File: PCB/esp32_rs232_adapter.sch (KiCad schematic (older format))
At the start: 8 parts

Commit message: work on schematics
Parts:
- removed C? (x4): CP1_Small, symbol Device:CP1_Small
- added C? (x4): 0.1uF, symbol Device:CP1_Small
- added C?: 1uF, symbol Device:CP1_Small
- added J?: DB9_Male, symbol Connector:DB9_Male
- added R? (x3): 1k, symbol Device:R_Small
- C?: value CP1_Small -> 0.1uF
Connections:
- net GND: now also U?.1 (GND), U?.15 (GND), U?.24 (IO2), U?.38 (GND), C?.1, C?.2, C?.2, C?.2, J?.5
- net RTS: now reaches U?.10 (T2IN)
- net RTS: now also U?.36 (IO22), R?.2
- net TXD: now reaches U?.11 (T1IN)
- net TXD: now also U?.35 (TXD0/IO1), R?.2
- net RXD: now reaches U?.12 (R1OUT)
- net RXD: now also U?.34 (RXD0/IO3)
- net RXD_RS232: now reaches J?.3, U?.13 (R1IN)
- net RXD_RS232: now also J?.2
- net TXD_RS232: now reaches J?.2, U?.14 (T1OUT)
- net TXD_RS232: now also J?.3
- net +3V3: now reaches U?.16 (VCC)
- net +3V3: now also U?.2 (VDD), C?.1, C?.1, R?.1, R?.1, R?.1
- net at U?.2 (VS+): now also C?.1
- net at U?.4 (C2+): now also C?.1
- net at U?.5 (C2-): now also C?.2
- net at U?.6 (VS-): now also C?.2
- net RTS_RS232: now reaches J?.8, U?.7 (T2OUT)
- net RTS_RS232: now also J?.7
- net CTS_RS232: now reaches J?.7, U?.8 (R2IN)
- net CTS_RS232: now also J?.8
- net CTS: now reaches U?.9 (R2OUT)
- net CTS: now also U?.31 (IO19)
- net at U?.25 (IO0): now also R?.2
- new net: J?.1, J?.4, J?.6
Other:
- moved on the sheet: C?, J?, U?

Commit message: Nearly finished schematic
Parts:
- removed R?: 1k, symbol Device:R_Small
- added D3, D4: LED_Small, LED_SMD:LED_0805_2012Metric, symbol Device:LED_Small
- added J1: Conn_01x04_Male, Connector_PinHeader_2.54mm:PinHeader_1x04_P2.54mm_Vertical, symbol Connector:Conn_01x04_Male
- added R1, R12, R13, R2, R5: 10k, Resistor_SMD:R_0805_2012Metric, symbol Device:R_Small
- added SW1: Flash, Button_Switch_SMD:SW_SPST_B3S-1000, symbol Switch:SW_Push
- C1: renamed from C?; value 1uF -> 10uF; footprint (none) -> Capacitor_SMD:C_0805_2012Metric
- C2, C3, C4, C5, C6: renamed from C?; footprint (none) -> Capacitor_SMD:C_0805_2012Metric
- J2: renamed from J?; value DB9_Male -> DB9; footprint (none) -> Connector_Dsub:DSUB-9_Male_Horizontal_P2.77x2.54mm_EdgePinOffset9.40mm; Supplier (none) -> https://www.aliexpress.com/item/DB9-Female-PCB-Mount-D-Sub-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
- J3: renamed from J?; value DB9_Male -> DB9X; footprint (none) -> Connector_Dsub:DSUB-9_Male_Horizontal_P2.77x2.54mm_EdgePinOffset9.40mm; Supplier (none) -> https://www.aliexpress.com/item/DB9-Female-PCB-Mount-D-Sub-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
- R3, R4: renamed from R?; value 1k -> 10k; footprint (none) -> Resistor_SMD:R_0805_2012Metric
- U1: renamed from U?; Supplier (none) -> https://www.aliexpress.com/item/ESP32-WROOM-32D-ESP32-D0WD-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
- U2: renamed from U?; footprint (none) -> Package_SO:SSOP-16_5.3x6.2mm_P0.65mm; Supplier (none) -> https://www.aliexpress.com/item/in-stock-can-pay-MAX3232CSE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
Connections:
- wire segments 93 -> 113
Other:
- moved on the sheet: C1, R3

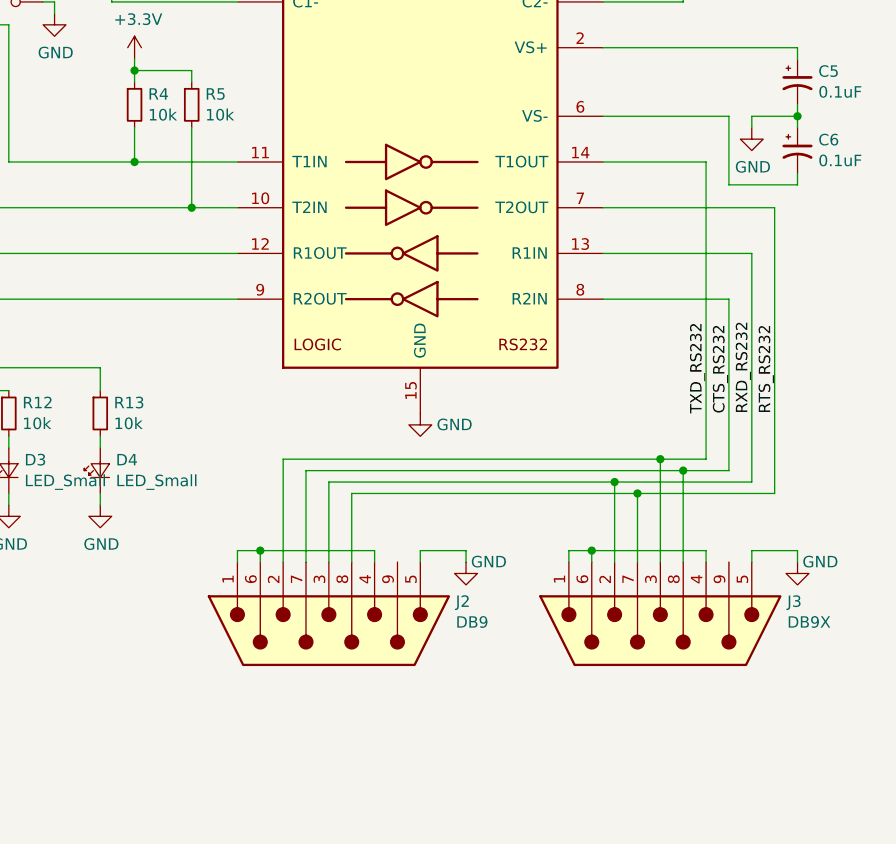
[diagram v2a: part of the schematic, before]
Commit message: change footprints. Add dip switch for null modem
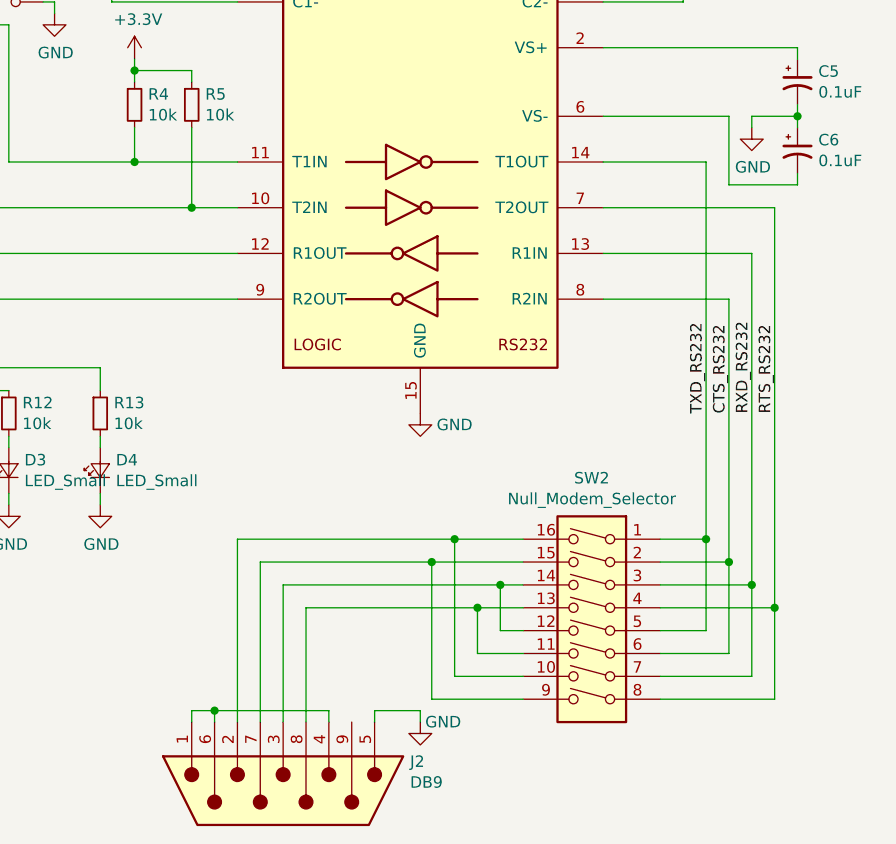
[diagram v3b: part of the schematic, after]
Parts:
- removed J3: DB9X, Connector_Dsub:DSUB-9_Male_Horizontal_P2.77x2.54mm_EdgePinOffset9.40mm, symbol Connector:DB9_Male
- added SW2: Null_Modem_Selector, Button_Switch_SMD:SW_DIP_SPSTx08_Slide_6.7x21.88mm_W8.61mm_P2.54mm_LowProfile, symbol Switch:SW_DIP_x08
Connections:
- wire segments 113 -> 121
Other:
- moved on the sheet: J2
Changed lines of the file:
@@
 L Connector:DB9_Male J2
 U 1 1 5C74F18C
-P 8600 5350
-F 0 "J2" V 8473 5905 50  0000 L CNN
-F 1 "DB9" V 8564 5905 50  0000 L CNN
-F 2 "Connector_Dsub:DSUB-9_Male_Horizontal_P2.77x2.54mm_EdgePinOffset9.40mm" H 8600 5350 50  0001 C CNN
-F 3 " ~" H 8600 5350 50  0001 C CNN
-F 4 "https://www.aliexpress.com/item/DB9-Female-PCB-Mount-D-Sub-9-pin-PCB-Connector-RS232-Connector-90-degree-bent-needle/32829295480.html" V 8600 5350 50  0001 C CNN "Supplier"
-	1    8600 5350
+P 8400 6050
+F 0 "J2" V 8273 6605 50  0000 L CNN
+F 1 "DB9" V 8364 6605 50  0000 L CNN
+F 2 "Connector_Dsub:DSUB-9_Male_Horizontal_P2.77x2.54mm_EdgePinOffset9.40mm" H 8400 6050 50  0001 C CNN
+F 3 " ~" H 8400 6050 50  0001 C CNN
+F 4 "https://www.aliexpress.com/item/DB9-Female-PCB-Mount-D-Sub-9-pin-PCB-Connector-RS232-Connector-90-degree-bent-needle/32829295480.html" V 8400 6050 50  0001 C CNN "Supplier"
+	1    8400 6050
 	0    1    1    0
 $EndComp
@@
 	10450 3100 10650 3100
 Wire Wire Line
-	8200 5050 8200 5000
-Wire Wire Line
-	8200 5000 8300 5000
-Wire Wire Line
-	8300 5000 8300 5050
-Wire Wire Line
-	8300 5000 8800 5000
-Wire Wire Line
-	8800 5000 8800 5050
-Connection ~ 8300 5000
-Wire Wire Line
-	9000 5050 9000 5000
-Wire Wire Line
-	9000 5000 9200 5000
+	8000 5750 8000 5700
+Wire Wire Line
+	8000 5700 8100 5700
+Wire Wire Line
+	8100 5700 8100 5750
+Wire Wire Line
+	8100 5700 8600 5700
+Wire Wire Line
+	8600 5700 8600 5750
+Connection ~ 8100 5700
+Wire Wire Line
+	8800 5750 8800 5700
+Wire Wire Line
+	8800 5700 9000 5700
 $Comp
 L power:GND #PWR014
 U 1 1 5C752181
-P 9200 5050
-F 0 "#PWR014" H 9200 4800 50  0001 C CNN
-F 1 "GND" H 9300 5050 50  0000 C CNN
-F 2 "" H 9200 5050 50  0001 C CNN
-F 3 "" H 9200 5050 50  0001 C CNN
-	1    9200 5050
-	1    0    0    -1
-$EndComp
-Wire Wire Line
-	8700 5050 8700 4750
-Wire Wire Line
-	10550 4750 10550 3500
+P 9000 5750
+F 0 "#PWR014" H 9000 5500 50  0001 C CNN
+F 1 "GND" H 9100 5750 50  0000 C CNN
+F 2 "" H 9000 5750 50  0001 C CNN
+F 3 "" H 9000 5750 50  0001 C CNN
+	1    9000 5750
+	1    0    0    -1
+$EndComp
+Wire Wire Line
+	8500 5750 8500 5250
 Wire Wire Line
 	10550 3500 9800 3500
@@
 	9800 3900 10350 3900
 Wire Wire Line
-	10350 3900 10350 4650
-Wire Wire Line
-	8500 4650 8500 5050
-Wire Wire Line
-	8400 5050 8400 4600
-Wire Wire Line
-	8400 4600 10050 4600
-Wire Wire Line
-	10250 4600 10250 3300
+	8200 5750 8200 4950
 Wire Wire Line
 	10250 3300 9800 3300
 Wire Wire Line
-	8600 5050 8600 4700
-Wire Wire Line
-	10450 4700 10450 3700
+	8400 5750 8400 5150
 Wire Wire Line
 	10450 3700 9800 3700
@@
 RTS_RS232
 Wire Wire Line
-	9200 5000 9200 5050
-$Comp
-L Connector:DB9_Male J3
-U 1 1 5C7F8A3E
-P 10050 5350
-F 0 "J3" V 9923 5905 50  0000 L CNN
-F 1 "DB9X" V 10014 5905 50  0000 L CNN
-F 2 "Connector_Dsub:DSUB-9_Male_Horizontal_P2.77x2.54mm_EdgePinOffset9.40mm" H 10050 5350 50  0001 C CNN
-F 3 " ~" H 10050 5350 50  0001 C CNN
-F 4 "https://www.aliexpress.com/item/DB9-Female-PCB-Mount-D-Sub-9-pin-PCB-Connector-RS232-Connector-90-degree-bent-needle/32829295480.html" V 10050 5350 50  0001 C CNN "Supplier"
-	1    10050 5350
-	0    1    1    0
-$EndComp
-Wire Wire Line
-	9650 5050 9650 5000
-Wire Wire Line
-	9650 5000 9750 5000
-Wire Wire Line
-	9750 5000 9750 5050
-Wire Wire Line
-	9750 5000 10250 5000
-Wire Wire Line
-	10250 5000 10250 5050
-Connection ~ 9750 5000
-Wire Wire Line
-	10450 5050 10450 5000
-Wire Wire Line
-	10450 5000 10650 5000
-$Comp
-L power:GND #PWR017
-U 1 1 5C7F8A4D
-P 10650 5050
-F 0 "#PWR017" H 10650 4800 50  0001 C CNN
-F 1 "GND" H 10750 5050 50  0000 C CNN
-F 2 "" H 10650 5050 50  0001 C CNN
-F 3 "" H 10650 5050 50  0001 C CNN
-	1    10650 5050
-	1    0    0    -1
-$EndComp
-Wire Wire Line
-	10650 5000 10650 5050
-Wire Wire Line
-	8500 4650 10150 4650
-Wire Wire Line
-	8700 4750 9950 4750
-Wire Wire Line
-	8600 4700 9850 4700
-Wire Wire Line
-	10250 4600 10050 4600
-Wire Wire Line
-	10050 4600 10050 5050
-Connection ~ 10050 4600
-Wire Wire Line
-	9850 4700 9850 5050
-Connection ~ 9850 4700
-Wire Wire Line
-	9850 4700 10450 4700
-Wire Wire Line
-	10150 4650 10150 5050
-Connection ~ 10150 4650
-Wire Wire Line
-	10150 4650 10350 4650
-Wire Wire Line
-	9950 4750 9950 5050
-Connection ~ 9950 4750
-Wire Wire Line
-	9950 4750 10550 4750
+	9000 5700 9000 5750
 $Comp
 L power:+3.3V #PWR04
@@
 	0    -1   -1   0
 $EndComp
+$Comp
+L Switch:SW_DIP_x08 SW2
+U 1 1 5C88E389
+P 9750 5350
+F 0 "SW2" H 9750 6017 50  0000 C CNN
+F 1 "Null_Modem_Selector" H 9750 5926 50  0000 C CNN
+F 2 "Button_Switch_SMD:SW_DIP_SPSTx08_Slide_6.7x21.88mm_W8.61mm_P2.54mm_LowProfile" H 9750 5350 50  0001 C CNN
+F 3 "https://www.aliexpress.com/item/10pcs-lot-Slide-Type-SMT-SMD-Dip-Switch-2-54mm-Pitch-2-Row-4-Pin-2/32956815576.html" H 9750 5350 50  0001 C CNN
+	1    9750 5350
+	-1   0    0    -1
+$EndComp
+Wire Wire Line
+	10250 4950 10050 4950
+Wire Wire Line
+	9450 4950 9150 4950
+Wire Wire Line
+	10250 3300 10250 4950
+Wire Wire Line
+	10250 4950 10250 5350
+Wire Wire Line
+	10250 5350 10050 5350
+Connection ~ 10250 4950
+Wire Wire Line
+	10350 5050 10050 5050
+Wire Wire Line
+	10350 5050 10350 5450
+Wire Wire Line
+	10350 5450 10050 5450
+Connection ~ 10350 5050
+Wire Wire Line
+	10450 5150 10050 5150
+Wire Wire Line
+	10450 5150 10450 5550
+Wire Wire Line
+	10450 5550 10050 5550
+Connection ~ 10450 5150
+Wire Wire Line
+	10550 5250 10050 5250
+Wire Wire Line
+	10550 5250 10550 5650
+Wire Wire Line
+	10550 5650 10050 5650
+Connection ~ 10550 5250
+Wire Wire Line
+	9450 5050 9050 5050
+Wire Wire Line
+	8300 5050 8300 5750
+Wire Wire Line
+	10350 3900 10350 5050
+Wire Wire Line
+	9450 5150 9350 5150
+Wire Wire Line
+	10450 3700 10450 5150
+Wire Wire Line
+	9450 5250 9250 5250
+Wire Wire Line
+	10550 3500 10550 5250
+Wire Wire Line
+	9450 5350 9350 5350
+Wire Wire Line
+	9350 5350 9350 5150
+Connection ~ 9350 5150
+Wire Wire Line
+	9350 5150 8400 5150
+Wire Wire Line
+	9450 5550 9150 5550
+Wire Wire Line
+	9150 5550 9150 4950
+Connection ~ 9150 4950
+Wire Wire Line
+	9150 4950 8200 4950
+Wire Wire Line
+	9450 5450 9250 5450
+Wire Wire Line
+	9250 5450 9250 5250
+Connection ~ 9250 5250
+Wire Wire Line
+	9250 5250 8500 5250
+Wire Wire Line
+	9450 5650 9050 5650
+Wire Wire Line
+	9050 5650 9050 5050
+Connection ~ 9050 5050
+Wire Wire Line
+	9050 5050 8300 5050
 $EndSCHEMATC

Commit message: PCB finished
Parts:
- added H1, H2, H3, H4: MountingHole, MountingHole:MountingHole_3.2mm_M3_ISO7380, symbol Mechanical:MountingHole
- J2: footprint Connector_Dsub:DSUB-9_Male_Horizontal_P2.77x2.54mm_EdgePinOffset9.40mm -> Connector_Dsub:DSUB-9_Male_Horizontal_P2.77x2.84mm_EdgePinOffset4.94mm_Housed_MountingHolesOffset7.48mm
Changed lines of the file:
@@
 F 0 "J2" V 8273 6605 50  0000 L CNN
 F 1 "DB9" V 8364 6605 50  0000 L CNN
-F 2 "Connector_Dsub:DSUB-9_Male_Horizontal_P2.77x2.54mm_EdgePinOffset9.40mm" H 8400 6050 50  0001 C CNN
+F 2 "Connector_Dsub:DSUB-9_Male_Horizontal_P2.77x2.84mm_EdgePinOffset4.94mm_Housed_MountingHolesOffset7.48mm" H 8400 6050 50  0001 C CNN
 F 3 " ~" H 8400 6050 50  0001 C CNN
 F 4 "https://www.aliexpress.com/item/DB9-Female-PCB-Mount-D-Sub-9-pin-PCB-Connector-RS232-Connector-90-degree-bent-needle/32829295480.html" V 8400 6050 50  0001 C CNN "Supplier"
@@
 Wire Wire Line
 	9050 5050 8300 5050
+$Comp
+L Mechanical:MountingHole H?
+U 1 1 5C979F20
+P 950 850
+AR Path="/5C7BB31A/5C979F20" Ref="H?"  Part="1"
+AR Path="/5C979F20" Ref="H1"  Part="1"
+F 0 "H1" H 1050 896 50  0000 L CNN
+F 1 "MountingHole" H 1050 805 50  0000 L CNN
+F 2 "MountingHole:MountingHole_3.2mm_M3_ISO7380" H 950 850 50  0001 C CNN
+F 3 "~" H 950 850 50  0001 C CNN
+	1    950  850
+	1    0    0    -1
+$EndComp
+$Comp
+L Mechanical:MountingHole H?
+U 1 1 5C979F27
+P 950 1050
+AR Path="/5C7BB31A/5C979F27" Ref="H?"  Part="1"
+AR Path="/5C979F27" Ref="H2"  Part="1"
+F 0 "H2" H 1050 1096 50  0000 L CNN
+F 1 "MountingHole" H 1050 1005 50  0000 L CNN
+F 2 "MountingHole:MountingHole_3.2mm_M3_ISO7380" H 950 1050 50  0001 C CNN
+F 3 "~" H 950 1050 50  0001 C CNN
+	1    950  1050
+	1    0    0    -1
+$EndComp
+$Comp
+L Mechanical:MountingHole H?
+U 1 1 5C979F2E
+P 950 1250
+AR Path="/5C7BB31A/5C979F2E" Ref="H?"  Part="1"
+AR Path="/5C979F2E" Ref="H3"  Part="1"
+F 0 "H3" H 1050 1296 50  0000 L CNN
+F 1 "MountingHole" H 1050 1205 50  0000 L CNN
+F 2 "MountingHole:MountingHole_3.2mm_M3_ISO7380" H 950 1250 50  0001 C CNN
+F 3 "~" H 950 1250 50  0001 C CNN
+	1    950  1250
+	1    0    0    -1
+$EndComp
+$Comp
+L Mechanical:MountingHole H?
+U 1 1 5C979F35
+P 950 1450
+AR Path="/5C7BB31A/5C979F35" Ref="H?"  Part="1"
+AR Path="/5C979F35" Ref="H4"  Part="1"
+F 0 "H4" H 1050 1496 50  0000 L CNN
+F 1 "MountingHole" H 1050 1405 50  0000 L CNN
+F 2 "MountingHole:MountingHole_3.2mm_M3_ISO7380" H 950 1450 50  0001 C CNN
+F 3 "~" H 950 1450 50  0001 C CNN
+	1    950  1450
+	1    0    0    -1
+$EndComp
 $EndSCHEMATC

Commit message: update
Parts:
- removed J1: Conn_01x04_Male, Connector_PinHeader_2.54mm:PinHeader_1x04_P2.54mm_Vertical, symbol Connector:Conn_01x04_Male
- U2: footprint Package_SO:SSOP-16_5.3x6.2mm_P0.65mm -> Package_SO:SOP-16_4.55x10.3mm_P1.27mm
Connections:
- wire segments 121 -> 126
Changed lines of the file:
@@
 EESchema Schematic File Version 4
 LIBS:esp32_rs232_adapter-cache
-EELAYER 26 0
+EELAYER 29 0
 EELAYER END
 $Descr A4 11693 8268
@@
 F 0 "U2" H 9000 4578 50  0000 C CNN
 F 1 "MAX3232" H 9000 4487 50  0000 C CNN
-F 2 "Package_SO:SSOP-16_5.3x6.2mm_P0.65mm" H 9050 2150 50  0001 L CNN
+F 2 "Package_SO:SOP-16_4.55x10.3mm_P1.27mm" H 9050 2150 50  0001 L CNN
 F 3 "https://datasheets.maximintegrated.com/en/ds/MAX3222-MAX3241.pdf" H 9000 3300 50  0001 C CNN
 F 4 "https://www.aliexpress.com/item/in-stock-can-pay-MAX3232CSE-MAX3232-MAX3232ESE-SOP-16/32821460559.html" H 9000 3200 50  0001 C CNN "Supplier"
@@
 F2 "3.3V" I R 3950 2500 50
 F3 "Vbatt_sig" I R 3950 2800 50
+F4 "power_status" I R 3950 3050 50
+F5 "charge_status" I R 3950 3150 50
 $EndSheet
 Wire Wire Line
@@
 Wire Wire Line
 	3950 2800 5400 2800
-$Comp
-L Connector:Conn_01x04_Male J1
-U 1 1 5C7F4A31
-P 2700 4350
-F 0 "J1" H 2806 4628 50  0000 C CNN
-F 1 "Conn_01x04_Male" H 2806 4537 50  0000 C CNN
-F 2 "Connector_PinHeader_2.54mm:PinHeader_1x04_P2.54mm_Vertical" H 2700 4350 50  0001 C CNN
-F 3 "~" H 2700 4350 50  0001 C CNN
-	1    2700 4350
-	1    0    0    -1
-$EndComp
-Wire Wire Line
-	2900 4250 3350 4250
-Wire Wire Line
-	2900 4350 3350 4350
-Wire Wire Line
-	2900 4550 3350 4550
-$Comp
-L power:GND #PWR01
-U 1 1 5C8018A8
-P 3350 4600
-F 0 "#PWR01" H 3350 4350 50  0001 C CNN
-F 1 "GND" H 3355 4427 50  0000 C CNN
-F 2 "" H 3350 4600 50  0001 C CNN
-F 3 "" H 3350 4600 50  0001 C CNN
-	1    3350 4600
-	1    0    0    -1
-$EndComp
-Wire Wire Line
-	3350 4600 3350 4550
-$Comp
-L power:+3.3V #PWR02
-U 1 1 5C804F12
-P 3550 4450
-F 0 "#PWR02" H 3550 4300 50  0001 C CNN
-F 1 "+3.3V" H 3565 4623 50  0000 C CNN
-F 2 "" H 3550 4450 50  0001 C CNN
-F 3 "" H 3550 4450 50  0001 C CNN
-	1    3550 4450
-	1    0    0    -1
-$EndComp
-Wire Wire Line
-	2900 4450 3550 4450
-Text Label 3350 4350 2    50   ~ 0
-TXD
-Text Label 3350 4250 2    50   ~ 0
-RXD
 $Comp
 L Device:LED_Small D3
@@
 	1    0    0    -1
 $EndComp
+Wire Wire Line
+	3950 3050 4800 3050
+Wire Wire Line
+	4800 3050 4800 5400
+Wire Wire Line
+	4800 5400 6700 5400
+Wire Wire Line
+	6700 5400 6700 4900
+Wire Wire Line
+	6700 4900 6600 4900
+Wire Wire Line
+	3950 3150 4700 3150
+Wire Wire Line
+	4700 3150 4700 5500
+Wire Wire Line
+	4700 5500 6750 5500
+Wire Wire Line
+	6750 5500 6750 4800
+Wire Wire Line
+	6750 4800 6600 4800
 $EndSCHEMATC

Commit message: work in progress with stuff for cb testing
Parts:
- added C12, C14, C17: 0.1uF, Capacitor_SMD:C_0805_2012Metric, symbol Device:CP1_Small
- added C13: 1nF, Capacitor_SMD:C_0805_2012Metric, symbol Device:CP1_Small
- added C15: 10nF, Capacitor_SMD:C_0805_2012Metric, symbol Device:CP1_Small
- added C16: 0.1nF, Capacitor_SMD:C_0805_2012Metric, symbol Device:CP1_Small
- added C18: 2.2nF, Capacitor_SMD:C_0805_2012Metric, symbol Device:CP1_Small
- added J3: Shunt-, Connector:Banana_Jack_1Pin, symbol Connector:Conn_01x01_Female
- added J4: Poles, Connector:Banana_Jack_3Pin, symbol Connector:Conn_01x03_Female
- added J5: Common, Connector:Banana_Jack_1Pin, symbol Connector:Conn_01x01_Female
- added J6: Shunt+, Connector:Banana_Jack_1Pin, symbol Connector:Conn_01x01_Female
- added R15: 3k3, Resistor_SMD:R_0805_2012Metric, symbol Device:R_Small
- added R16, R17, R18: 10k, Resistor_SMD:R_0805_2012Metric, symbol Device:R_Small
- added U5: ACS712xLCTR-30A, Package_SO:SOIC-8_3.9x4.9mm_P1.27mm, symbol Sensor_Current:ACS712xLCTR-30A
- added U6: MPU-6050, Sensor_Motion:InvenSense_QFN-24_4x4mm_P0.5mm, symbol Sensor_Motion:MPU-6050
- U1: footprint RF_Module:ESP32-WROOM-32 -> power_supplies:ESP32-WROOM-32-Heat
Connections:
- net labels added: Aph, Bph, ChargePwrStatus, ChargeStatus, Cph, External+, External-, I_sense, Vbatt_sig, mpu_INT, mpu_SCL, mpu_SDA
- wire segments 126 -> 194
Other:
- moved on the sheet: C1, C2, C3, C4, C5, C6, D3, D4, J2, R1, R12, R13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

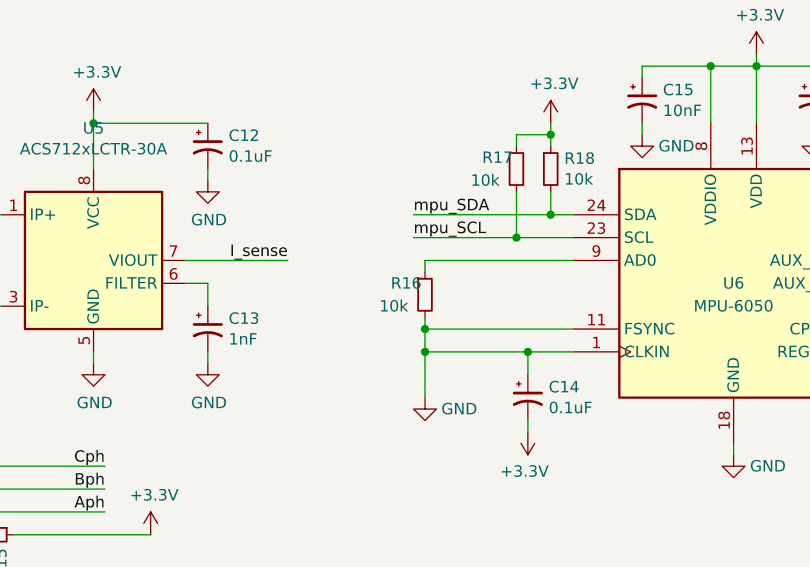
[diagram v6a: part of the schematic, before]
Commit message: Updated pin assignments
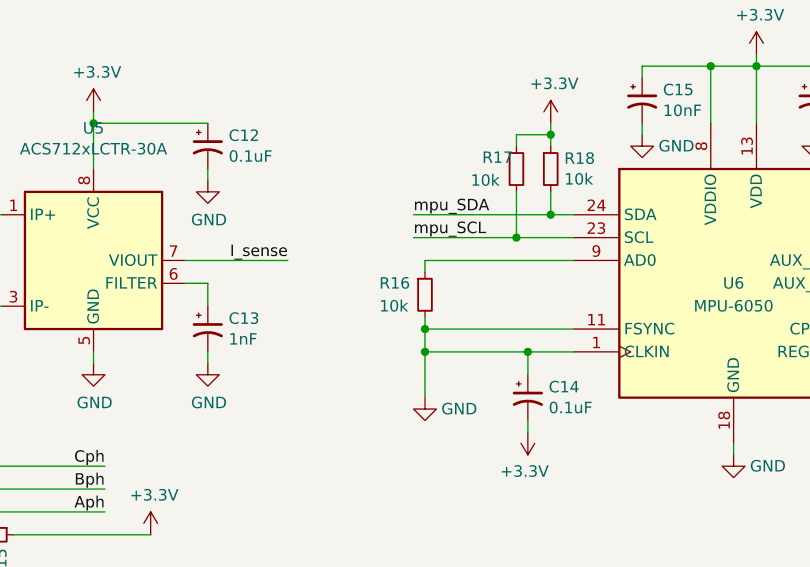
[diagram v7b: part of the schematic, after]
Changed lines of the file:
@@
 U 1 1 5CF9B26F
 P 3650 6500
-F 0 "R16" H 3500 6550 50  0000 L CNN
+F 0 "R16" H 3450 6550 50  0000 L CNN
 F 1 "10k" H 3450 6450 50  0000 L CNN
 F 2 "Resistor_SMD:R_0805_2012Metric" H 3650 6500 50  0001 C CNN
